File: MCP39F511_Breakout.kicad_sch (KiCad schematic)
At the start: 25 parts, among them J1 Conn_01x10, U1 MCP39F511-E_MQ, U2 MCP9700T-ETT, Y1 Crystal

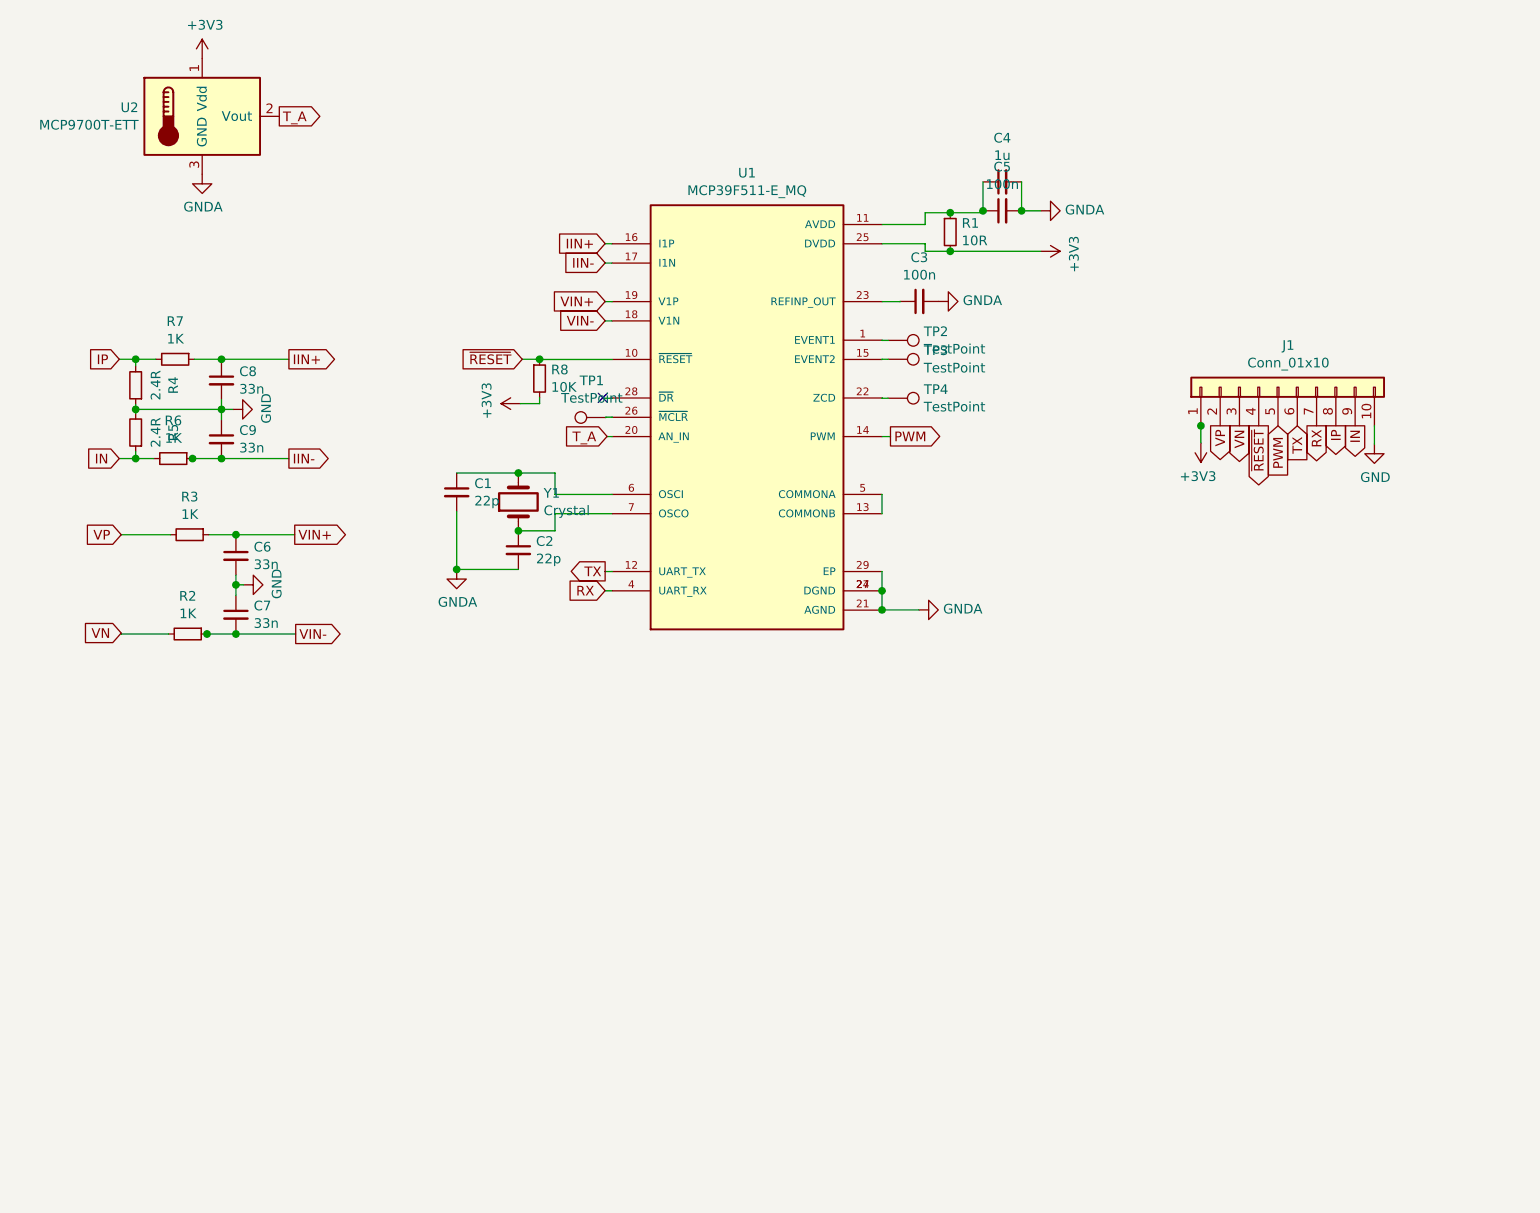
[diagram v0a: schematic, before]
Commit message: Finish routing and silk-screens
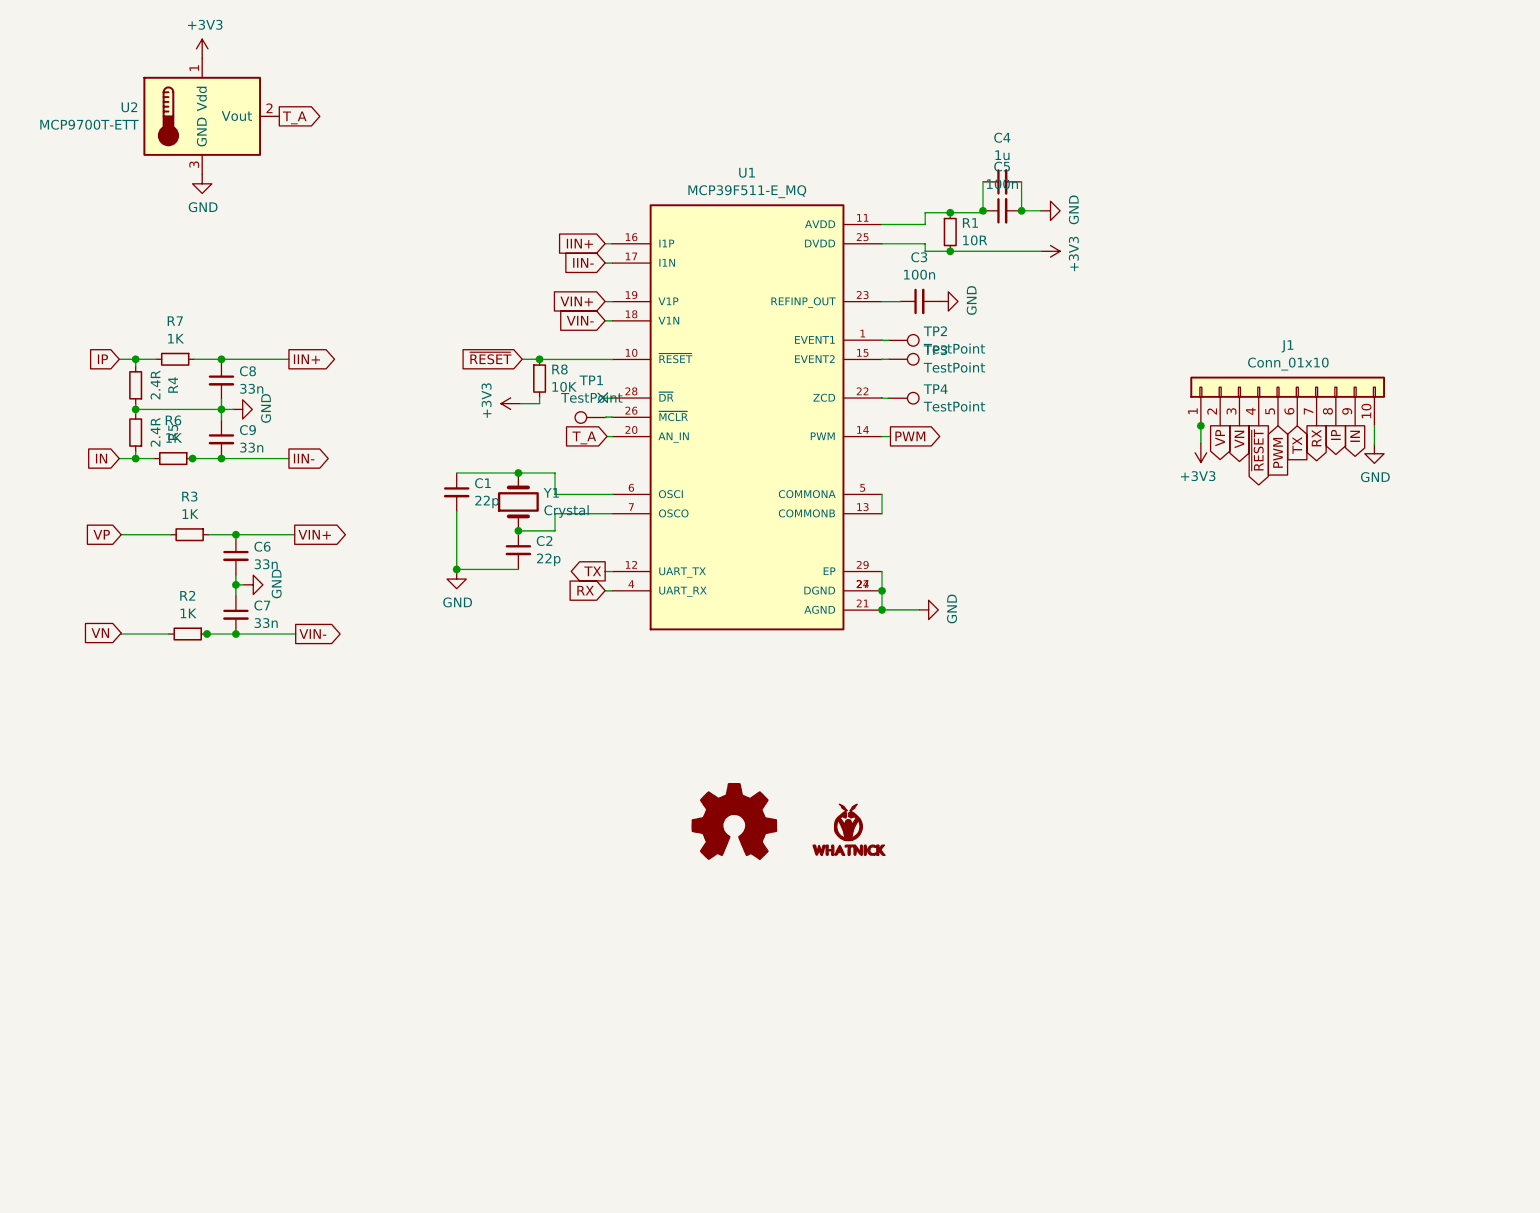
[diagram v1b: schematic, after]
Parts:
- added LOGO1: Logo_Open_Hardware_Small, Symbol:OSHW-Logo2_7.3x6mm_SilkScreen, symbol Graphic:Logo_Open_Hardware_Small
- added LOGO2: LOGO, Whatnick_logo:Whatnick_logo, symbol whatnick:LOGO
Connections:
- net GNDA is gone; now on net GND: C1.2, C2.2, C3.2, C4.2, C5.2, U1.21 (AGND), U1.24 (DGND), U1.27 (DGND), U1.29 (EP), U2.3 (GND)
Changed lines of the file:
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@@
     )
   )
-  (symbol (lib_id "power:GNDA") (at 62.23 51.054 0) (unit 1)
+  (symbol (lib_id "power:GND") (at 62.23 51.054 0) (unit 1)
     (in_bom yes) (on_board yes)
     (property "Reference" "#PWR0112" (id 0) (at 62.23 57.404 0)
       (effects (font (size 1.27 1.27)) hide)
     )
-    (property "Value" "GNDA" (id 1) (at 62.3443 55.3784 0))
+    (property "Value" "GND" (id 1) (at 62.357 55.4482 0))
     (property "Footprint" "" (id 2) (at 62.23 51.054 0)
       (effects (font (size 1.27 1.27)) hide)
@@
     )
   )
-  (symbol (lib_id "power:GNDA") (at 95.758 103.124 0) (unit 1)
+  (symbol (lib_id "power:GND") (at 95.758 103.124 0) (unit 1)
     (in_bom yes) (on_board yes)
     (property "Reference" "#PWR0107" (id 0) (at 95.758 109.474 0)
       (effects (font (size 1.27 1.27)) hide)
     )
-    (property "Value" "GNDA" (id 1) (at 95.8723 107.4484 0))
+    (property "Value" "GND" (id 1) (at 95.885 107.5182 0))
     (property "Footprint" "" (id 2) (at 95.758 103.124 0)
       (effects (font (size 1.27 1.27)) hide)
@@
     )
   )
-  (symbol (lib_id "power:GNDA") (at 156.6672 108.458 90) (unit 1)
+  (symbol (lib_id "power:GND") (at 156.6672 108.458 90) (unit 1)
     (in_bom yes) (on_board yes)
     (property "Reference" "#PWR0104" (id 0) (at 163.0172 108.458 0)
       (effects (font (size 1.27 1.27)) hide)
     )
-    (property "Value" "GNDA" (id 1) (at 159.8423 108.3437 90)
-      (effects (font (size 1.27 1.27)) (justify right))
-    )
+    (property "Value" "GND" (id 1) (at 161.0614 108.331 0))
     (property "Footprint" "" (id 2) (at 156.6672 108.458 0)
       (effects (font (size 1.27 1.27)) hide)
@@
     )
   )
-  (symbol (lib_id "power:GNDA") (at 159.258 67.818 90) (unit 1)
+  (symbol (lib_id "power:GND") (at 159.258 67.818 90) (unit 1)
     (in_bom yes) (on_board yes)
     (property "Reference" "#PWR0103" (id 0) (at 165.608 67.818 0)
       (effects (font (size 1.27 1.27)) hide)
     )
-    (property "Value" "GNDA" (id 1) (at 162.4331 67.7037 90)
-      (effects (font (size 1.27 1.27)) (justify right))
-    )
+    (property "Value" "GND" (id 1) (at 163.6522 67.691 0))
     (property "Footprint" "" (id 2) (at 159.258 67.818 0)
       (effects (font (size 1.27 1.27)) hide)
@@
     )
   )
-  (symbol (lib_id "power:GNDA") (at 172.72 55.88 90) (unit 1)
+  (symbol (lib_id "power:GND") (at 172.72 55.88 90) (unit 1)
     (in_bom yes) (on_board yes)
     (property "Reference" "#PWR0105" (id 0) (at 179.07 55.88 0)
       (effects (font (size 1.27 1.27)) hide)
     )
-    (property "Value" "GNDA" (id 1) (at 175.8951 55.7657 90)
-      (effects (font (size 1.27 1.27)) (justify right))
-    )
+    (property "Value" "GND" (id 1) (at 177.1142 55.753 0))
     (property "Footprint" "" (id 2) (at 172.72 55.88 0)
       (effects (font (size 1.27 1.27)) hide)
@@
     )
     (property "Datasheet" "~" (id 3) (at 103.886 94.234 0)
+      (effects (font (size 1.27 1.27)) hide)
+    )
+  )
+  (symbol (lib_id "whatnick:LOGO") (at 147.4216 137.414 0) (unit 1)
+    (in_bom yes) (on_board yes)
+    (property "Reference" "LOGO2" (id 0) (at 147.4216 140.0048 0)
+      (effects (font (size 1.524 1.524)) hide)
+    )
+    (property "Value" "LOGO" (id 1) (at 147.4216 134.8232 0)
+      (effects (font (size 1.524 1.524)) hide)
+    )
+    (property "Footprint" "Whatnick_logo:Whatnick_logo" (id 2) (at 147.4216 137.414 0)
+      (effects (font (size 1.27 1.27)) hide)
+    )
+    (property "Datasheet" "" (id 3) (at 147.4216 137.414 0)
+      (effects (font (size 1.27 1.27)) hide)
+    )
+  )
+  (symbol (lib_id "Graphic:Logo_Open_Hardware_Small") (at 132.334 136.9568 0) (unit 1)
+    (in_bom yes) (on_board yes)
+    (property "Reference" "LOGO1" (id 0) (at 132.334 129.9718 0)
+      (effects (font (size 1.27 1.27)) hide)
+    )
+    (property "Value" "Logo_Open_Hardware_Small" (id 1) (at 132.334 142.6718 0)
+      (effects (font (size 1.27 1.27)) hide)
+    )
+    (property "Footprint" "Symbol:OSHW-Logo2_7.3x6mm_SilkScreen" (id 2) (at 132.334 136.9568 0)
+      (effects (font (size 1.27 1.27)) hide)
+    )
+    (property "Datasheet" "~" (id 3) (at 132.334 136.9568 0)
       (effects (font (size 1.27 1.27)) hide)
     )
@@
       (reference "#PWR0102") (unit 1) (value "GND") (footprint "")
     )
-    (path "/547d650d-c998-48e0-8bb5-38b14317f755"
-      (reference "#PWR0103") (unit 1) (value "GNDA") (footprint "")
-    )
-    (path "/92f0311f-4ef9-40e9-9943-18aa866ae0d2"
-      (reference "#PWR0104") (unit 1) (value "GNDA") (footprint "")
-    )
-    (path "/6ebc934d-20aa-4a60-ae44-f85f6afe0cd6"
-      (reference "#PWR0105") (unit 1) (value "GNDA") (footprint "")
+    (path "/bccf2043-ab1c-4993-9e9e-8bc3e0e48c48"
+      (reference "#PWR0103") (unit 1) (value "GND") (footprint "")
+    )
+    (path "/56e094b5-1676-4160-8f5b-923476c22325"
+      (reference "#PWR0104") (unit 1) (value "GND") (footprint "")
+    )
+    (path "/c95a14fc-15fb-4d07-9d2d-8ea966d0b380"
+      (reference "#PWR0105") (unit 1) (value "GND") (footprint "")
     )
     (path "/7d1614a3-e6e4-4c36-96c7-78bf35978939"
       (reference "#PWR0106") (unit 1) (value "+3V3") (footprint "")
     )
-    (path "/51414145-efa5-4faa-8090-ed24f8db0cbd"
-      (reference "#PWR0107") (unit 1) (value "GNDA") (footprint "")
+    (path "/e734b6c3-c3c9-4e5a-ba2e-5b14968b4174"
+      (reference "#PWR0107") (unit 1) (value "GND") (footprint "")
     )
     (path "/e231b0e2-1a94-4df9-bbda-202fba246edb"
@@
       (reference "#PWR0111") (unit 1) (value "+3V3") (footprint "")
     )
-    (path "/46bcb6ae-3c4a-4ac4-a6c9-ff20092a9e55"
-      (reference "#PWR0112") (unit 1) (value "GNDA") (footprint "")
+    (path "/233734c2-4923-4a84-9411-b819f69768cf"
+      (reference "#PWR0112") (unit 1) (value "GND") (footprint "")
     )
     (path "/d567969e-8cf4-4a83-a4af-95a8e2ea4ba9"
@@
       (reference "J1") (unit 1) (value "Conn_01x10") (footprint "Connector_PinHeader_2.54mm:PinHeader_1x10_P2.54mm_Vertical")
     )
+    (path "/825baacd-881a-4969-bcf1-0132eae8d96d"
+      (reference "LOGO1") (unit 1) (value "Logo_Open_Hardware_Small") (footprint "Symbol:OSHW-Logo2_7.3x6mm_SilkScreen")
+    )
+    (path "/4e8c3968-23ed-4647-b65c-e125a5fb82f6"
+      (reference "LOGO2") (unit 1) (value "LOGO") (footprint "Whatnick_logo:Whatnick_logo")
+    )
     (path "/ca4014b1-2c9b-46f1-99e4-a467f6e4a53b"

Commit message: Do an iBOM run
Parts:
- C1, C2: manf# (none) -> C0603C220M4RACTU
- C3, C5: manf# (none) -> C0603C104K4PACTU
- C4: manf# (none) -> C0603C105K4PAC7411
- J1, LOGO1, LOGO2, TP1, TP2, TP3, TP4: DNP (none) -> ...
- R1: manf# (none) -> RC0603FR-0710RP
- R8: manf# (none) -> RC0603FR-0710KL
- U2: manf# (none) -> MCP9700T-E/TT
- Y1: value Crystal -> 4MHz / 16pF; manf# (none) -> LFXTAL003071Reel
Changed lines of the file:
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@@
+      (effects (font (size 1.27 1.27)) hide)
+    )
+    (property "DNP" "..." (id 4) (at 115.4176 83.1088 0)
       (effects (font (size 1.27 1.27)) hide)
     )
@@
       (effects (font (size 1.27 1.27)) hide)
     )
+    (property "DNP" "..." (id 4) (at 152.6032 72.9488 0)
+      (effects (font (size 1.27 1.27)) hide)
+    )
   )
   (symbol (lib_id "Connector:TestPoint") (at 152.6032 75.438 270) (unit 1)
@@
       (effects (font (size 1.27 1.27)) hide)
     )
+    (property "DNP" "..." (id 4) (at 152.6032 75.438 0)
+      (effects (font (size 1.27 1.27)) hide)
+    )
   )
   (symbol (lib_id "Connector:TestPoint") (at 152.6032 80.5688 270) (unit 1)
@@
     )
     (property "Datasheet" "~" (id 3) (at 152.6032 85.6488 0)
+      (effects (font (size 1.27 1.27)) hide)
+    )
+    (property "DNP" "..." (id 4) (at 152.6032 80.5688 0)
       (effects (font (size 1.27 1.27)) hide)
     )
@@
       (effects (font (size 1.27 1.27)) hide)
     )
+    (property "manf#" "RC0603FR-0710KL" (id 4) (at 106.68 77.978 0)
+      (effects (font (size 1.27 1.27)) hide)
+    )
   )
   (symbol (lib_id "Device:R_Small") (at 160.782 58.674 0) (unit 1)
@@
       (effects (font (size 1.27 1.27)) hide)
     )
+    (property "manf#" "RC0603FR-0710RP" (id 4) (at 160.782 58.674 0)
+      (effects (font (size 1.27 1.27)) hide)
+    )
   )
   (symbol (lib_id "Device:C_Small") (at 64.77 78.232 0) (unit 1)
@@
       (effects (font (size 1.27 1.27)) hide)
     )
+    (property "manf#" "C0603C220M4RACTU" (id 4) (at 95.758 92.964 0)
+      (effects (font (size 1.27 1.27)) hide)
+    )
   )
   (symbol (lib_id "Device:C_Small") (at 103.886 100.584 0) (unit 1)
@@
     )
     (property "Datasheet" "~" (id 3) (at 103.886 100.584 0)
+      (effects (font (size 1.27 1.27)) hide)
+    )
+    (property "manf#" "C0603C220M4RACTU" (id 4) (at 103.886 100.584 0)
       (effects (font (size 1.27 1.27)) hide)
     )
@@
       (effects (font (size 1.27 1.27)) hide)
     )
+    (property "manf#" "C0603C104K4PACTU" (id 4) (at 156.718 67.818 0)
+      (effects (font (size 1.27 1.27)) hide)
+    )
   )
   (symbol (lib_id "Device:C_Small") (at 167.64 52.07 90) (unit 1)
@@
       (effects (font (size 1.27 1.27)) hide)
     )
+    (property "manf#" "C0603C105K4PAC7411" (id 4) (at 167.64 52.07 0)
+      (effects (font (size 1.27 1.27)) hide)
+    )
   )
   (symbol (lib_id "Device:C_Small") (at 167.64 55.88 90) (unit 1)
@@
       (effects (font (size 1.27 1.27)) hide)
     )
+    (property "manf#" "C0603C104K4PACTU" (id 4) (at 167.64 55.88 0)
+      (effects (font (size 1.27 1.27)) hide)
+    )
   )
   (symbol (lib_id "Device:Crystal") (at 103.886 94.234 90) (unit 1)
@@
       (effects (font (size 1.27 1.27)) (justify right))
     )
-    (property "Value" "Crystal" (id 1) (at 107.2135 95.3833 90)
+    (property "Value" "4MHz / 16pF" (id 1) (at 107.2135 95.3833 90)
       (effects (font (size 1.27 1.27)) (justify right))
     )
@@
     )
     (property "Datasheet" "~" (id 3) (at 103.886 94.234 0)
+      (effects (font (size 1.27 1.27)) hide)
+    )
+    (property "manf#" "LFXTAL003071Reel" (id 4) (at 103.886 94.234 0)
       (effects (font (size 1.27 1.27)) hide)
     )
@@
       (effects (font (size 1.27 1.27)) hide)
     )
+    (property "DNP" "..." (id 4) (at 147.4216 137.414 0)
+      (effects (font (size 1.27 1.27)) hide)
+    )
   )
   (symbol (lib_id "Graphic:Logo_Open_Hardware_Small") (at 132.334 136.9568 0) (unit 1)
@@
     )
     (property "Datasheet" "~" (id 3) (at 132.334 136.9568 0)
+      (effects (font (size 1.27 1.27)) hide)
+    )
+    (property "DNP" "..." (id 4) (at 132.334 136.9568 0)
       (effects (font (size 1.27 1.27)) hide)
     )
@@
       (effects (font (size 1.27 1.27)) hide)
     )
-    (property "DNP" " " (id 4) (at 203.962 79.121 0)
+    (property "DNP" "..." (id 4) (at 203.962 79.121 0)
       (effects (font (size 1.27 1.27)) hide)
     )
@@
     )
     (property "Datasheet" "http://ww1.microchip.com/downloads/en/DeviceDoc/21942e.pdf" (id 3) (at 58.42 37.084 0)
+      (effects (font (size 1.27 1.27)) hide)
+    )
+    (property "manf#" "MCP9700T-E/TT" (id 4) (at 62.23 43.434 0)
       (effects (font (size 1.27 1.27)) hide)
     )
@@
     )
     (path "/79f19a69-5faa-4a2d-b9ce-765ab89483de"
-      (reference "Y1") (unit 1) (value "Crystal") (footprint "Crystal:Crystal_SMD_HC49-SD")
-    )
-  )
+      (reference "Y1") (unit 1) (value "4MHz / 16pF") (footprint "Crystal:Crystal_SMD_HC49-SD")
+    )
+  )

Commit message: Do a MPN included iBOM run
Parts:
- U1: manf# (none) -> MCP39F511-E/MQ
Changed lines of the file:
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@@
       (effects (font (size 1.27 1.27)) (justify left bottom) hide)
+    )
+    (property "manf#" "MCP39F511-E/MQ" (id 4) (at 134.0104 83.0834 0)
+      (effects (font (size 1.27 1.27)) hide)
     )
   )

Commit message: Update BOM
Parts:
- C6, C7, C8, C9: manf# 06035C273MAT2A -> 0603YC333KAT2A
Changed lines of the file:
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@@
       (effects (font (size 1.27 1.27)) hide)
     )
-    (property "manf#" "06035C273MAT2A" (id 4) (at 64.77 78.232 0)
+    (property "manf#" "0603YC333KAT2A" (id 4) (at 64.77 78.232 0)
       (effects (font (size 1.27 1.27)) hide)
     )
@@
       (effects (font (size 1.27 1.27)) hide)
     )
-    (property "manf#" "06035C273MAT2A" (id 4) (at 64.77 85.979 0)
+    (property "manf#" "0603YC333KAT2A" (id 4) (at 64.77 85.979 0)
       (effects (font (size 1.27 1.27)) hide)
     )
@@
       (effects (font (size 1.27 1.27)) hide)
     )
-    (property "manf#" "06035C273MAT2A" (id 4) (at 66.675 101.346 0)
+    (property "manf#" "0603YC333KAT2A" (id 4) (at 66.675 101.346 0)
       (effects (font (size 1.27 1.27)) hide)
     )
@@
       (effects (font (size 1.27 1.27)) hide)
     )
-    (property "manf#" "06035C273MAT2A" (id 4) (at 66.675 109.093 0)
+    (property "manf#" "0603YC333KAT2A" (id 4) (at 66.675 109.093 0)
       (effects (font (size 1.27 1.27)) hide)
     )
